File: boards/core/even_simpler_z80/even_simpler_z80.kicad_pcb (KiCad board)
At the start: 2 copper layers, 95.2 x 95.2 mm, 41 parts, among them J1 Exp. Conn. A, J2 Exp. Conn. B, J3 Power, J4 EXT_CLK, J5 CPU_CLK_SEL, J6 BUS_CLK_SEL, U1 Z80CPPLC44, U2 74LS32, U3 74LS244, U4 74LS04, U5 74LS244, U6 74LS244, U7 74LS08, U8 74LS245, X1 INT_CLK

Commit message: * Working on new powerdistribution method.
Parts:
- removed C10: 0.1uF, Capacitor_THT:C_Disc_D5.0mm_W2.5mm_P2.50mm
- added C9: 0.1uF, Capacitor_THT:C_Disc_D5.0mm_W2.5mm_P2.50mm, F.Cu at (47.5, 64.3)
- D2: value 1N4148 -> 1N4148
- R1: value 1k -> 470
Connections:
- net /A16 renamed /M_A14
- net /A17 renamed /M_A15
- net /A18 renamed /M_A16
- net /A19 renamed /M_A17
- net /A20 renamed /M_A18
- net /A21 renamed /M_A19
- net /A22 renamed /M_A20
- net /A23 renamed /M_A21

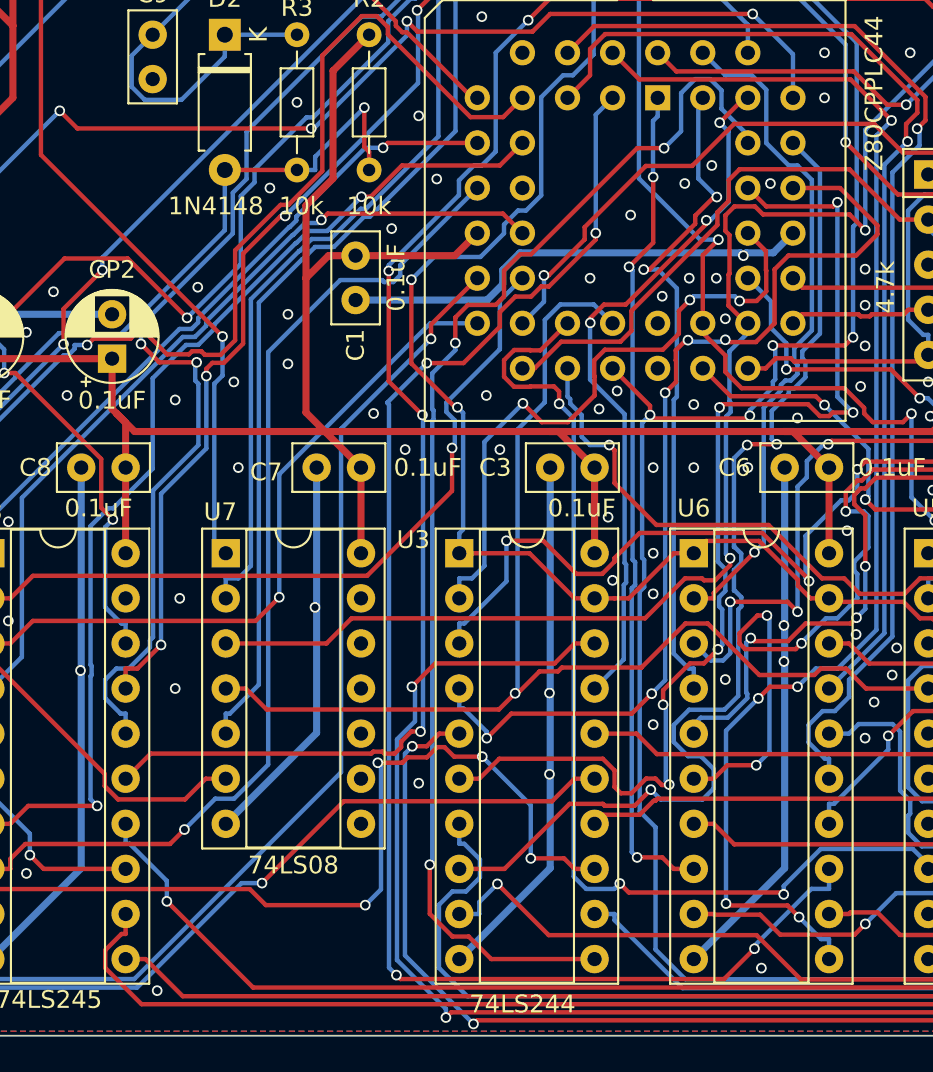
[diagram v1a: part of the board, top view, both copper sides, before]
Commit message: Added expansion connector C and designed some new boards around it.
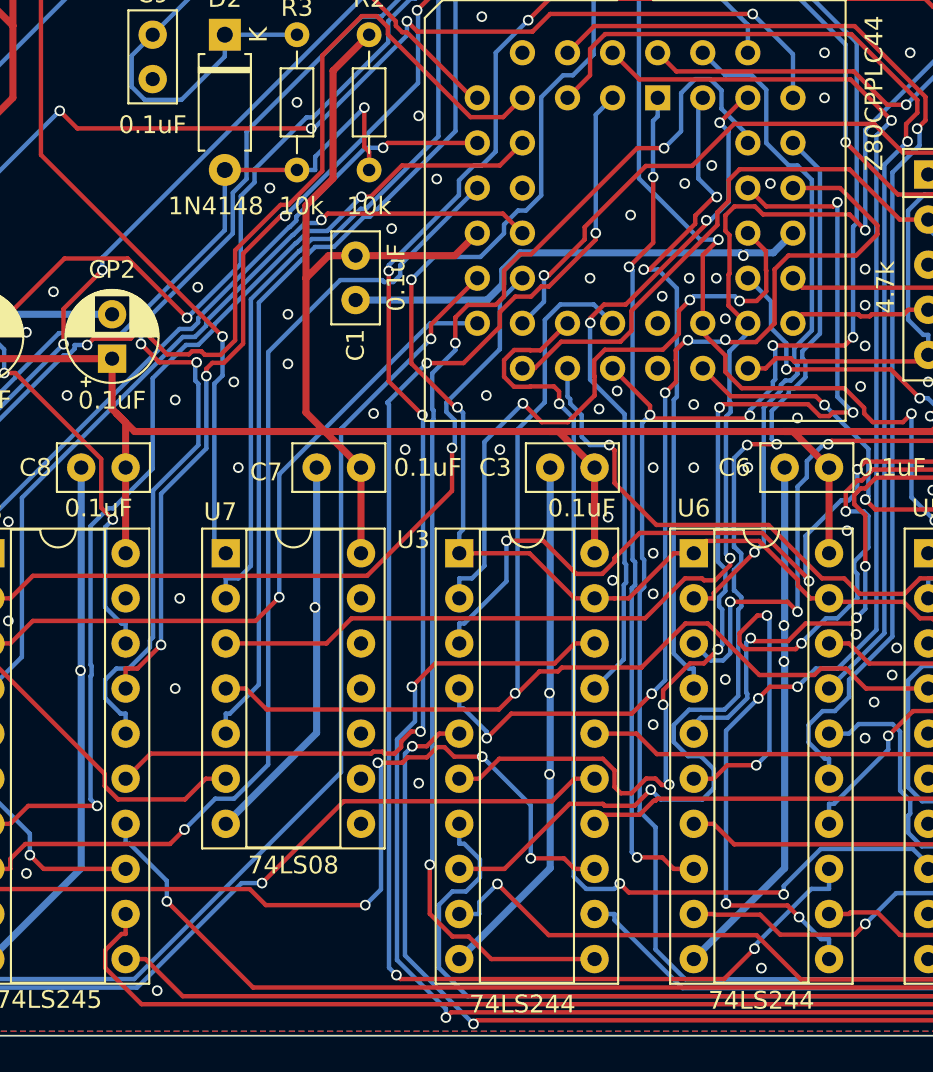
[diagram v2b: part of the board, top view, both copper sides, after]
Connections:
- net Net-(D2-K) renamed /Clock & Reset circuit/~{RESET_IN}
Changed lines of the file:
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@@
   (net 1 "/+5V")
   (net 2 "/GND")
-  (net 3 "Net-(D2-K)")
+  (net 3 "/Clock & Reset circuit/~{RESET_IN}")
   (net 4 "Net-(D1-A)")
   (net 5 "/~{RESET_SW}")
@@
         (effects (font (size 1 1) (thickness 0.15)))
     )
-    (fp_text value "74LS244" (at 3.81 25.19) (layer "F.Fab")
+    (fp_text value "74LS244" (at 3.81 25.19) (layer "F.SilkS")
         (effects (font (size 1 1) (thickness 0.15)))
     )
@@
       (stroke (width 0.1) (type solid)) (layer "F.Fab"))
     (pad "1" thru_hole rect (at 0 0 270) (size 1.8 1.8) (drill 0.9) (layers "*.Cu" "*.Mask")
-      (net 3 "Net-(D2-K)") (pinfunction "K") (pintype "passive"))
+      (net 3 "/Clock & Reset circuit/~{RESET_IN}") (pinfunction "K") (pintype "passive"))
     (pad "2" thru_hole oval (at 7.62 0 270) (size 1.8 1.8) (drill 0.9) (layers "*.Cu" "*.Mask")
       (net 5 "/~{RESET_SW}") (pinfunction "A") (pintype "passive"))
@@
       (stroke (width 0.1) (type solid)) (layer "F.Fab"))
     (pad "1" thru_hole circle (at 0 0 270) (size 1.4 1.4) (drill 0.7) (layers "*.Cu" "*.Mask")
-      (net 3 "Net-(D2-K)") (pintype "passive"))
+      (net 3 "/Clock & Reset circuit/~{RESET_IN}") (pintype "passive"))
     (pad "2" thru_hole oval (at 7.62 0 270) (size 1.4 1.4) (drill 0.7) (layers "*.Cu" "*.Mask")
       (net 5 "/~{RESET_SW}") (pintype "passive"))
@@
         (effects (font (size 1 1) (thickness 0.15)))
     )
-    (fp_text value "0.1uF" (at 5.08 0 -180) (layer "F.Fab")
+    (fp_text value "0.1uF" (at 5.08 0 180) (layer "F.SilkS")
         (effects (font (size 1 1) (thickness 0.15)))
     )
@@
       (stroke (width 0.1) (type solid)) (layer "F.Fab"))
     (pad "1" thru_hole circle (at 0 0 270) (size 1.6 1.6) (drill 0.8) (layers "*.Cu" "*.Mask")
-      (net 3 "Net-(D2-K)") (pintype "passive"))
+      (net 3 "/Clock & Reset circuit/~{RESET_IN}") (pintype "passive"))
     (pad "2" thru_hole circle (at 2.5 0 270) (size 1.6 1.6) (drill 0.8) (layers "*.Cu" "*.Mask")
       (net 2 "/GND") (pintype "passive"))
@@
       (stroke (width 0.1) (type solid)) (layer "F.Fab"))
     (pad "1" thru_hole rect (at 0 0) (size 1.6 1.6) (drill 0.8) (layers "*.Cu" "*.Mask")
-      (net 3 "Net-(D2-K)") (pintype "input"))
+      (net 3 "/Clock & Reset circuit/~{RESET_IN}") (pintype "input"))
     (pad "2" thru_hole oval (at 0 2.54) (size 1.6 1.6) (drill 0.8) (layers "*.Cu" "*.Mask")
       (net 43 "/Clock & Reset circuit/RESET1") (pintype "output"))
